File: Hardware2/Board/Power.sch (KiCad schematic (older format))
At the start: 22 parts

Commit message: Finished schematic
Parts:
- removed C?: 330u, symbol C
- removed C?: 10u/36V, symbol C
- removed C? (x2): 220p, symbol C
- removed C?: 22n, symbol C
- removed C? (x2): 4u7, symbol C
- removed D? (x3): STPS340U, symbol D
- removed L? (x2): 15u, symbol L_Small
- removed R?: 4k7, symbol R
- removed R?: 10k, symbol R
- removed R?: 3k3, symbol R
- removed R?: 117k, symbol R
- removed R?: 13k3, symbol R
- removed U?: L5973D, symbol L5973D
- removed U?: LM27313, symbol LM27313
- added C10, C12, C7: 22u, Capacitors_SMD:C_0805, symbol C
- added C11, C6, C9: 10u/25V/X7R, Capacitors_SMD:C_1206, symbol C
- added P21, P22, P23, P24, P27, P28: CONN_01X01, LedControl:Pad, symbol CONN_01X01
- added P25, P29: CONN_01X02, LedControl:WAGO_2060-452, symbol CONN_01X02
- added P30: CONN_01X02, LedControl:WAGO_2059-302, symbol CONN_01X02
- added P31, P32: CONN_01X05, LedControl:LED_Strip, symbol CONN_01X05
- added R10, R6, R8: 523k, Resistors_SMD:R_0603, symbol R
- added R11, R7, R9: 100k, Resistors_SMD:R_0603, symbol R
- added U4, U6, U8: TPS82130, LedControl:TPS82130, symbol TPS82130
- added U7: SP3485CN, Housings_SOIC:SOIC-8_3.9x4.9mm_Pitch1.27mm, symbol SP3485CN
- C8: renamed from C?; value 4u7 -> 22u; footprint (none) -> Capacitors_SMD:C_0805
- P26: renamed from P?; footprint (none) -> LedControl:WAGO_2060-452
- U5: renamed from U?; footprint (none) -> TO_SOT_Packages_SMD:SOT-23-5
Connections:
- net labels added: VCC
- net labels removed: +12V, EN12V, VPP
- wire segments 61 -> 102
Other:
- note added: "5V"
- note added: "7-16V"
- note added: "DATA"
- note added: "GND"
- note added: "R1"
- note added: "R1 = (Vout/0.8V - 1) * R2"
- note added: "R2"
- note added: "Vout = 0.8V x (1+R1/R2)"
- note removed: "1.235V"
- note removed: "3.3V -> 5k6\n5V -> 10k"
- note removed: "5-36V"

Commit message: Finished routing main board
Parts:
- added D2, D3: SS 12L, Diodes_SMD:D_1206, symbol D
- added J4, J5, J6: J, LedControl:Jumper, symbol CONN_01X02
- P20: renamed from P21; value CONN_01X01 -> TP
- P21: renamed from P22; value CONN_01X01 -> TP
- P22: renamed from P23; value CONN_01X01 -> TP
- P23: renamed from P24; value CONN_01X01 -> TP
- P24: renamed from P25; value CONN_01X02 -> 2060-452
- P25: renamed from P26; value CONN_01X02 -> 2060-452
- P26: renamed from P27; value CONN_01X01 -> TP
- P27: renamed from P28; value CONN_01X01 -> TP
- P28: renamed from P29; value CONN_01X02 -> 2060-452
- P29: renamed from P30; value CONN_01X02 -> 2059-302
- P30: renamed from P31; value CONN_01X05 -> LED_Strip
- U8: renamed from U7; value SP3485CN -> SP485CN
- renumbered P32 to P31, R6 to R12, R7 to R13, R8 to R14, R9 to R15, R10 to R16, R11 to R17, U4 to U5, U5 to U6, U6 to U7, U8 to U9
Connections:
- wire segments 102 -> 110
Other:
- note added: "15V"
- note added: "Test Pads"

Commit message: routing nearly finished
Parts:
- added C13, C14: 100n, Capacitors_SMD:C_0603, symbol C
- added R18, R19: 52k3, Resistors_SMD:R_0603, symbol R
- added R20, R21: 10k, Resistors_SMD:R_0603, symbol R
- C11, C6, C9: value 10u/25V/X7R -> 10u
- P30: footprint LedControl:LED_Strip -> LedControl:LED_Strip_Start
- P31: value CONN_01X05 -> LED_Strip
- R12, R14, R16: value 523k -> 52k3
- R13, R15, R17: value 100k -> 10k
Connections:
- net labels added: U1, U2
- wire segments 110 -> 144
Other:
- note added: "10u: use 25V/X7R"
- note added: "Connections get broken on PCB"

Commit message: Update to KiCad 5.0.1, add debug connector
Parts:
- C10, C12, C7, C8: footprint Capacitors_SMD:C_0805 -> Capacitor_SMD:C_0805_2012Metric; symbol C -> Device:C
- C11, C6, C9: footprint Capacitors_SMD:C_1206 -> Capacitor_SMD:C_1206_3216Metric; symbol C -> Device:C
- C13, C14: footprint Capacitors_SMD:C_0603 -> Capacitor_SMD:C_0603_1608Metric; symbol C -> Device:C
- D2, D3: footprint Diodes_SMD:D_1206 -> Diode_SMD:D_1206_3216Metric; symbol D -> Device:D
- J4, J5, J6, P24, P25, P28, P29: symbol CONN_01X02 -> Connector_Generic:Conn_01x02
- P20, P21, P22, P23, P26, P27: symbol CONN_01X01 -> Connector_Generic:Conn_01x01
- P30, P31: symbol CONN_01X05 -> Connector_Generic:Conn_01x05
- R12, R13, R14, R15, R16, R17, R18, R19, R20, R21: footprint Resistors_SMD:R_0603 -> Resistor_SMD:R_0603_1608Metric; symbol R -> Device:R
- U5, U7, U9: symbol TPS82130 -> Regulator_Switching:TPS82130
- U6: footprint TO_SOT_Packages_SMD:SOT-23-5 -> Package_TO_SOT_SMD:SOT-23-5; symbol LP2985LV -> Regulator_Linear:LP2985-3.3
- U8: footprint Housings_SOIC:SOIC-8_3.9x4.9mm_Pitch1.27mm -> Package_SO:SOIC-8_3.9x4.9mm_P1.27mm; symbol SP3485CN -> Interface_UART:SP3485CN
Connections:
- wire segments 144 -> 201

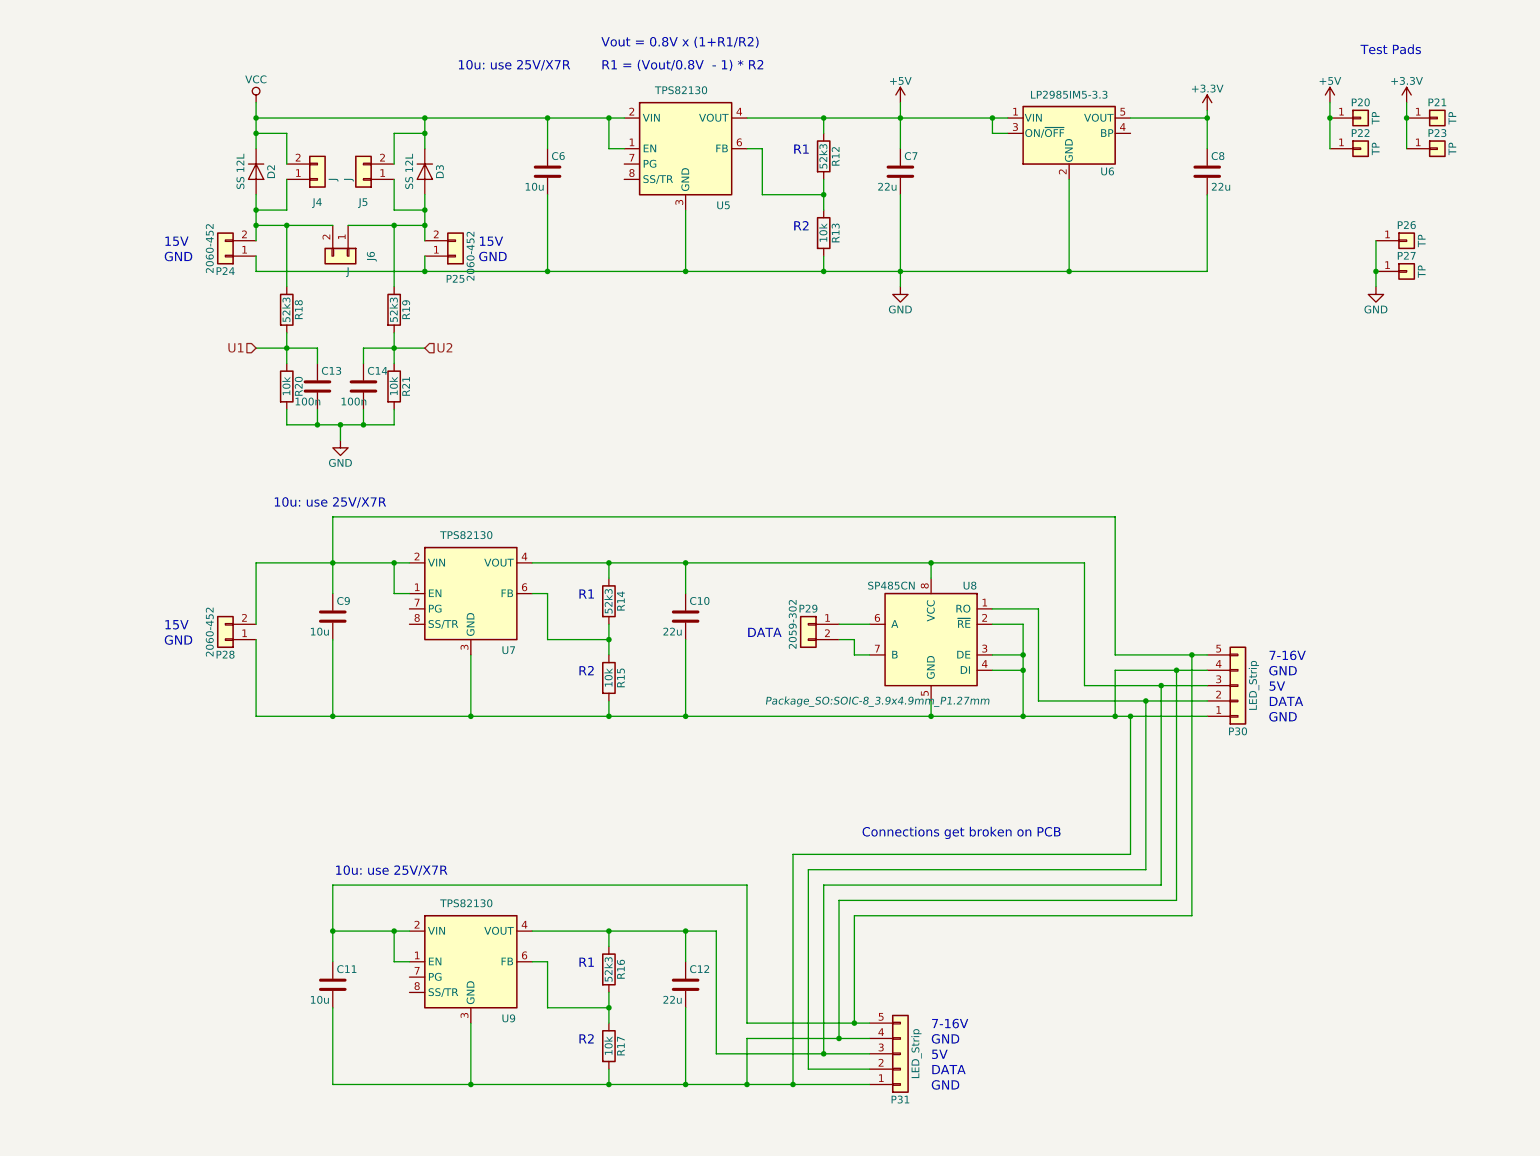
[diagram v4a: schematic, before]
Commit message: LED strip power supply below strip
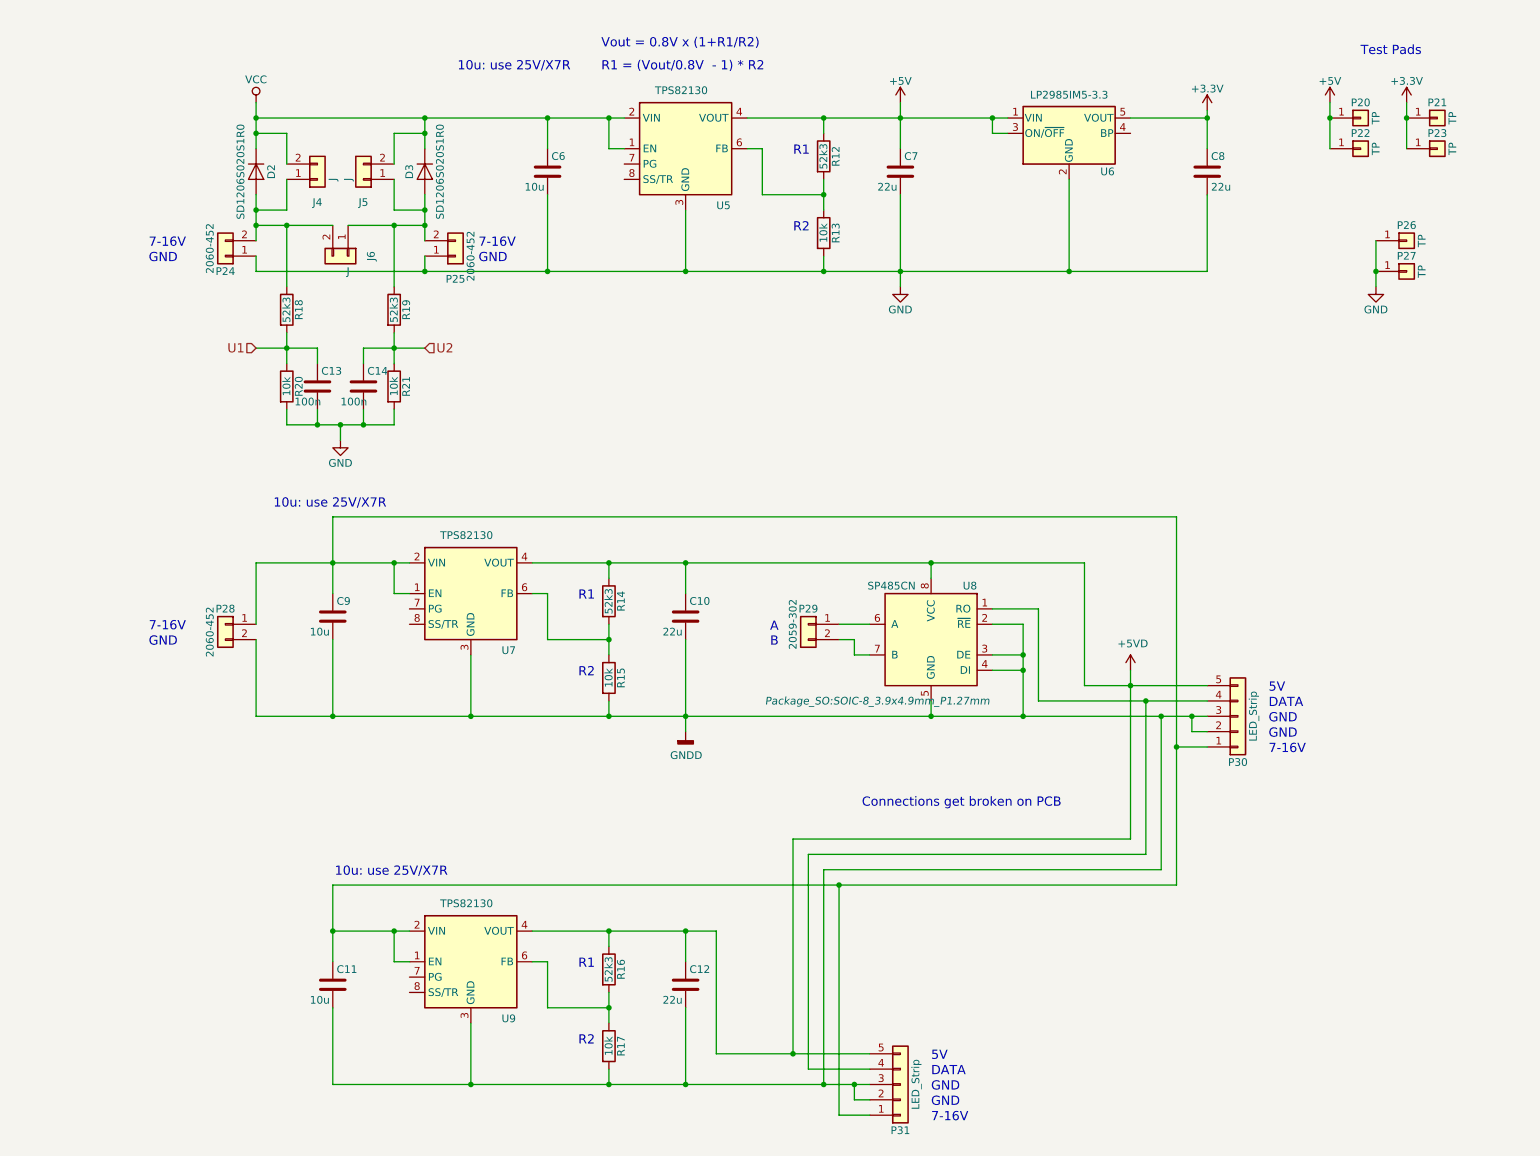
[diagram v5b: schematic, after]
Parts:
- D2, D3: value SS 12L -> SD1206S020S1R0
- P30: footprint LedControl:LED_Strip_Start -> LedControl:LED_Strip
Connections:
- net at C11.1, C9.1, U7.1 (EN)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: now also P28.1 (Pin_1), P30.1 (Pin_1), P31.1 (Pin_1); no longer P28.2 (Pin_2), P30.5 (Pin_5), P31.5 (Pin_5)
- net GNDD: now reaches C10.2, C11.2, C12.2, C9.2, R15.2, R17.2, U7.3 (GND), U7.9 (GND), U8.2 (~RE~), U8.3 (DE), U8.4 (DI), U8.5 (GND), U9.3 (GND), U9.9 (GND)
- net GNDD: now also P28.2 (Pin_2), P30.2 (Pin_2), P30.3 (Pin_3), P31.2 (Pin_2), P31.3 (Pin_3); no longer P28.1 (Pin_1), P30.1 (Pin_1), P30.4 (Pin_4), P31.1 (Pin_1), P31.4 (Pin_4)
- net +5VD: now reaches C10.1, C12.1, R14.1, R16.1, U7.4 (VOUT), U7.5 (VOUT), U8.8 (VCC), U9.4 (VOUT), U9.5 (VOUT)
- net +5VD: now also P30.5 (Pin_5), P31.5 (Pin_5); no longer P30.3 (Pin_3), P31.3 (Pin_3)
- new net: P30.4 (Pin_4), P31.4 (Pin_4), U8.1 (RO)
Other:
- note added: "A\nB"
- note removed: "15V"
- moved on the sheet: P30, P31
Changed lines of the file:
@@
 LIBS:LedControl-rescue
 LIBS:power
-LIBS:device
-LIBS:74xx
-LIBS:audio
-LIBS:interface
 LIBS:LedControl
 LIBS:LedControl-cache
@@
 	1    0    0    -1
 $EndComp
-Text Notes 1400 1950 0    60   ~ 0
-15V
+Text Notes 1300 1950 0    60   ~ 0
+7-16V
 $Comp
 L Regulator_Linear:LP2985-3.3 U6
@@
 	1    0    0    -1
 $EndComp
-Text Notes 6400 7050 0    60   ~ 0
+Text Notes 6400 7650 0    60   ~ 0
 7-16V
 Text Notes 6400 7250 0    60   ~ 0
@@
 L Connector_Generic:Conn_01x02 P28
 U 1 1 5A6BAEA8
-P 1800 4500
-F 0 "P28" H 1800 4600 50  0000 C CNN
-F 1 "2060-452" V 1900 4450 50  0000 C CNN
-F 2 "LedControl:WAGO_2060-452" H 1800 4500 50  0001 C CNN
-F 3 "" H 1800 4500 50  0000 C CNN
-	1    1800 4500
-	-1   0    0    1
+P 1800 4400
+F 0 "P28" H 1800 4500 50  0000 C CNN
+F 1 "2060-452" V 1900 4350 50  0000 C CNN
+F 2 "LedControl:WAGO_2060-452" H 1800 4400 50  0001 C CNN
+F 3 "" H 1800 4400 50  0000 C CNN
+	1    1800 4400
+	-1   0    0    -1
 $EndComp
 $Comp
@@
 	-1   0    0    -1
 $EndComp
-Text Notes 1400 4450 0    60   ~ 0
-15V
+Text Notes 1300 4450 0    60   ~ 0
+7-16V
 $Comp
 L Interface_UART:SP3485CN U8
@@
 	-1   0    0    -1
 $EndComp
-Text Notes 8600 4650 0    60   ~ 0
+Text Notes 8600 5250 0    60   ~ 0
 7-16V
-Text Notes 8600 4750 0    60   ~ 0
+Text Notes 8600 5150 0    60   ~ 0
 GND
 Text Notes 8600 4850 0    60   ~ 0
@@
 Text Notes 6400 7450 0    60   ~ 0
 GND
-Text Notes 1400 4550 0    60   ~ 0
+Text Notes 1300 4550 0    60   ~ 0
 GND
-Text Notes 1400 2050 0    60   ~ 0
+Text Notes 1300 2050 0    60   ~ 0
 GND
-Text Notes 5200 4500 0    60   ~ 0
-DATA
+Text Notes 5350 4550 0    60   ~ 0
+A\nB
 $Comp
 L Connector_Generic:Conn_01x05 P30
 U 1 1 5A760B4F
-P 8400 4800
-F 0 "P30" H 8400 5100 50  0000 C CNN
-F 1 "LED_Strip" V 8500 4800 50  0000 C CNN
-F 2 "LedControl:LED_Strip_Start" H 8400 4800 50  0001 C CNN
-F 3 "" H 8400 4800 50  0000 C CNN
-	1    8400 4800
+P 8400 5000
+F 0 "P30" H 8400 5300 50  0000 C CNN
+F 1 "LED_Strip" V 8500 5000 50  0000 C CNN
+F 2 "LedControl:LED_Strip" H 8400 5000 50  0001 C CNN
+F 3 "" H 8400 5000 50  0000 C CNN
+	1    8400 5000
 	1    0    0    1
 $EndComp
@@
 L Connector_Generic:Conn_01x05 P31
 U 1 1 5A7616D5
-P 6200 7200
-F 0 "P31" H 6200 7500 50  0000 C CNN
-F 1 "LED_Strip" V 6300 7200 50  0000 C CNN
-F 2 "LedControl:LED_Strip" H 6200 7200 50  0001 C CNN
-F 3 "" H 6200 7200 50  0000 C CNN
-	1    6200 7200
+P 6200 7400
+F 0 "P31" H 6200 7700 50  0000 C CNN
+F 1 "LED_Strip" V 6300 7400 50  0000 C CNN
+F 2 "LedControl:LED_Strip" H 6200 7400 50  0001 C CNN
+F 3 "" H 6200 7400 50  0000 C CNN
+	1    6200 7400
 	1    0    0    1
 $EndComp
 Text Notes 6400 7350 0    60   ~ 0
 DATA
-Text Notes 6400 7150 0    60   ~ 0
+Text Notes 6400 7550 0    60   ~ 0
 GND
 Text Notes 4250 800  0    60   ~ 0
@@
 P 2000 1450
 F 0 "D2" H 2000 1550 50  0000 C CNN
-F 1 "SS 12L" H 2000 1350 50  0000 C CNN
+F 1 "SD1206S020S1R0" H 2000 1350 50  0000 C CNN
 F 2 "Diode_SMD:D_1206_3216Metric" H 2000 1450 50  0001 C CNN
 F 3 "" H 2000 1450 50  0000 C CNN
@@
 U 1 1 5AA70BEB
 P 3100 1450
-F 0 "D3" H 3100 1550 50  0000 C CNN
-F 1 "SS 12L" H 3100 1350 50  0000 C CNN
+F 0 "D3" H 3100 1350 50  0000 C CNN
+F 1 "SD1206S020S1R0" H 3100 1550 50  0000 C CNN
 F 2 "Diode_SMD:D_1206_3216Metric" H 3100 1450 50  0001 C CNN
 F 3 "" H 3100 1450 50  0000 C CNN
@@
 	2000 4000 2000 4400
 Wire Wire Line
-	2000 4500 2000 5000
-Wire Wire Line
 	6400 5000 6400 4900
 Connection ~ 4800 5000
@@
 	7400 4000 7400 4800
 Wire Wire Line
-	7400 4800 7900 4800
-Wire Wire Line
-	7600 4700 8000 4700
-Wire Wire Line
-	7600 4700 7600 5000
-Connection ~ 7600 5000
+	7400 4800 7700 4800
 Wire Wire Line
 	2500 3700 2500 4000
 Wire Wire Line
-	2500 3700 7600 3700
-Wire Wire Line
-	7600 3700 7600 4600
-Wire Wire Line
-	7600 4600 8100 4600
-Wire Wire Line
-	5000 7200 5700 7200
+	5000 7200 5500 7200
 Wire Wire Line
 	5000 6400 5000 7200
-Wire Wire Line
-	2500 6100 5200 6100
-Wire Wire Line
-	5200 6100 5200 7000
-Wire Wire Line
-	5200 7000 5900 7000
-Wire Wire Line
-	5200 7100 5800 7100
-Wire Wire Line
-	5200 7100 5200 7400
-Connection ~ 5200 7400
 Wire Wire Line
 	2000 2000 2000 2100
@@
 U2
 Text Notes 3450 1950 0    60   ~ 0
-15V
+7-16V
 Text Notes 3450 2050 0    60   ~ 0
 GND
 Wire Wire Line
-	8100 4600 8100 6300
-Wire Wire Line
-	8100 6300 5900 6300
-Wire Wire Line
-	5900 6300 5900 7000
-Connection ~ 5900 7000
-Connection ~ 8100 4600
-Wire Wire Line
-	8000 4700 8000 6200
-Wire Wire Line
-	8000 6200 5800 6200
-Wire Wire Line
-	5800 6200 5800 7100
-Connection ~ 5800 7100
-Connection ~ 8000 4700
-Wire Wire Line
-	7900 4800 7900 6100
-Wire Wire Line
-	7900 6100 5700 6100
-Wire Wire Line
-	5700 6100 5700 7200
-Connection ~ 5700 7200
-Connection ~ 7900 4800
-Wire Wire Line
-	7800 4900 7800 6000
-Wire Wire Line
-	7800 6000 5600 6000
-Wire Wire Line
-	5600 6000 5600 7300
+	7700 4800 7700 5800
+Wire Wire Line
+	7700 5800 5500 5800
+Wire Wire Line
+	5500 5800 5500 7200
+Connection ~ 5500 7200
+Connection ~ 7700 4800
+Wire Wire Line
+	7800 4900 7800 5900
+Wire Wire Line
+	7800 5900 5600 5900
+Wire Wire Line
+	5600 5900 5600 7300
 Wire Wire Line
 	5600 7300 6000 7300
 Connection ~ 7800 4900
 Wire Wire Line
-	7700 5000 7700 5900
-Wire Wire Line
-	7700 5900 5500 5900
-Wire Wire Line
-	5500 5900 5500 7400
-Connection ~ 5500 7400
-Connection ~ 7700 5000
-Text Notes 7250 5800 2    60   ~ 0
+	7900 5000 7900 6000
+Wire Wire Line
+	7900 6000 5700 6000
+Wire Wire Line
+	5700 6000 5700 7400
+Connection ~ 5700 7400
+Connection ~ 7900 5000
+Text Notes 7250 5600 2    60   ~ 0
 Connections get broken on PCB
 Text Notes 4050 800  2    60   ~ 0
@@
 	2500 6400 2500 6600
 Wire Wire Line
-	4800 7400 5200 7400
-Wire Wire Line
 	4800 6400 5000 6400
 Wire Wire Line
@@
 	6400 4000 7400 4000
 Wire Wire Line
-	7000 5000 7600 5000
-Wire Wire Line
 	7000 4600 7000 4700
 Wire Wire Line
 	7000 4700 7000 5000
 Wire Wire Line
-	7600 5000 7700 5000
-Wire Wire Line
-	5200 7400 5500 7400
-Wire Wire Line
 	3100 2100 3900 2100
 Wire Wire Line
@@
 	2550 3100 2700 3100
 Wire Wire Line
-	5900 7000 6000 7000
-Wire Wire Line
-	8100 4600 8200 4600
-Wire Wire Line
-	5800 7100 6000 7100
-Wire Wire Line
-	8000 4700 8200 4700
-Wire Wire Line
-	5700 7200 6000 7200
-Wire Wire Line
-	7900 4800 8200 4800
+	5500 7200 6000 7200
+Wire Wire Line
+	7700 4800 8200 4800
 Wire Wire Line
 	7800 4900 8200 4900
 Wire Wire Line
-	5500 7400 6000 7400
-Wire Wire Line
-	7700 5000 8200 5000
+	5700 7400 5900 7400
+Wire Wire Line
+	7900 5000 8100 5000
 Wire Wire Line
 	6200 2100 7300 2100
@@
 	2900 6400 3000 6400
 Connection ~ 2900 6400
+$Comp
+L power:GNDD #PWR0102
+U 1 1 5C7C8E53
+P 4800 5100
+F 0 "#PWR0102" H 4800 4850 50  0001 C CNN
+F 1 "GNDD" H 4804 4945 50  0000 C CNN
+F 2 "" H 4800 5100 50  0001 C CNN
+F 3 "" H 4800 5100 50  0001 C CNN
+	1    4800 5100
+	1    0    0    -1
+$EndComp
+$Comp
+L power:+5VD #PWR0103
+U 1 1 5C7C9990
+P 7700 4700
+F 0 "#PWR0103" H 7700 4550 50  0001 C CNN
+F 1 "+5VD" H 7715 4873 50  0000 C CNN
+F 2 "" H 7700 4700 50  0001 C CNN
+F 3 "" H 7700 4700 50  0001 C CNN
+	1    7700 4700
+	1    0    0    -1
+$EndComp
+Wire Wire Line
+	4800 5100 4800 5000
+Wire Wire Line
+	7000 5000 7900 5000
+Wire Wire Line
+	8100 5000 8100 5100
+Wire Wire Line
+	8100 5100 8200 5100
+Connection ~ 8100 5000
+Wire Wire Line
+	8100 5000 8200 5000
+Wire Wire Line
+	2500 3700 8000 3700
+Wire Wire Line
+	8000 3700 8000 5200
+Wire Wire Line
+	8200 5200 8000 5200
+Connection ~ 8000 5200
+Wire Wire Line
+	8000 5200 8000 6100
+Wire Wire Line
+	5900 7400 5900 7500
+Wire Wire Line
+	5900 7500 6000 7500
+Connection ~ 5900 7400
+Wire Wire Line
+	5900 7400 6000 7400
+Wire Wire Line
+	2500 6100 5800 6100
+Wire Wire Line
+	4800 7400 5700 7400
+Wire Wire Line
+	6000 7600 5800 7600
+Wire Wire Line
+	5800 7600 5800 6100
+Connection ~ 5800 6100
+Wire Wire Line
+	5800 6100 8000 6100
+Wire Wire Line
+	2000 4500 2000 5000
+Wire Wire Line
+	7700 4800 7700 4700
 $EndSCHEMATC

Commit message: Add CAN bus
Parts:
- removed J4, J5: J, LedControl:Jumper, symbol Connector_Generic:Conn_01x02
- added P35: 2060-452, LedControl:WAGO_2060-452, symbol Connector_Generic:Conn_01x02
- J7: renamed from J6; value J -> Jumper
- renumbered P22 to P21, P21 to P22, R20 to R19, R19 to R20
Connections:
- net GNDD: now also P35.1 (Pin_1)
- net at C11.1, C9.1, P28.1 (Pin_1)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: now also P35.2 (Pin_2)
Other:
- moved on the sheet: C10, C11, C12, C9, J7, P20, P21, P22, P23, P26, P27, P31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
